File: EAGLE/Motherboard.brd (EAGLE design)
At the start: 60.9 x 49.2 mm, 16 parts, among them T1 BC337

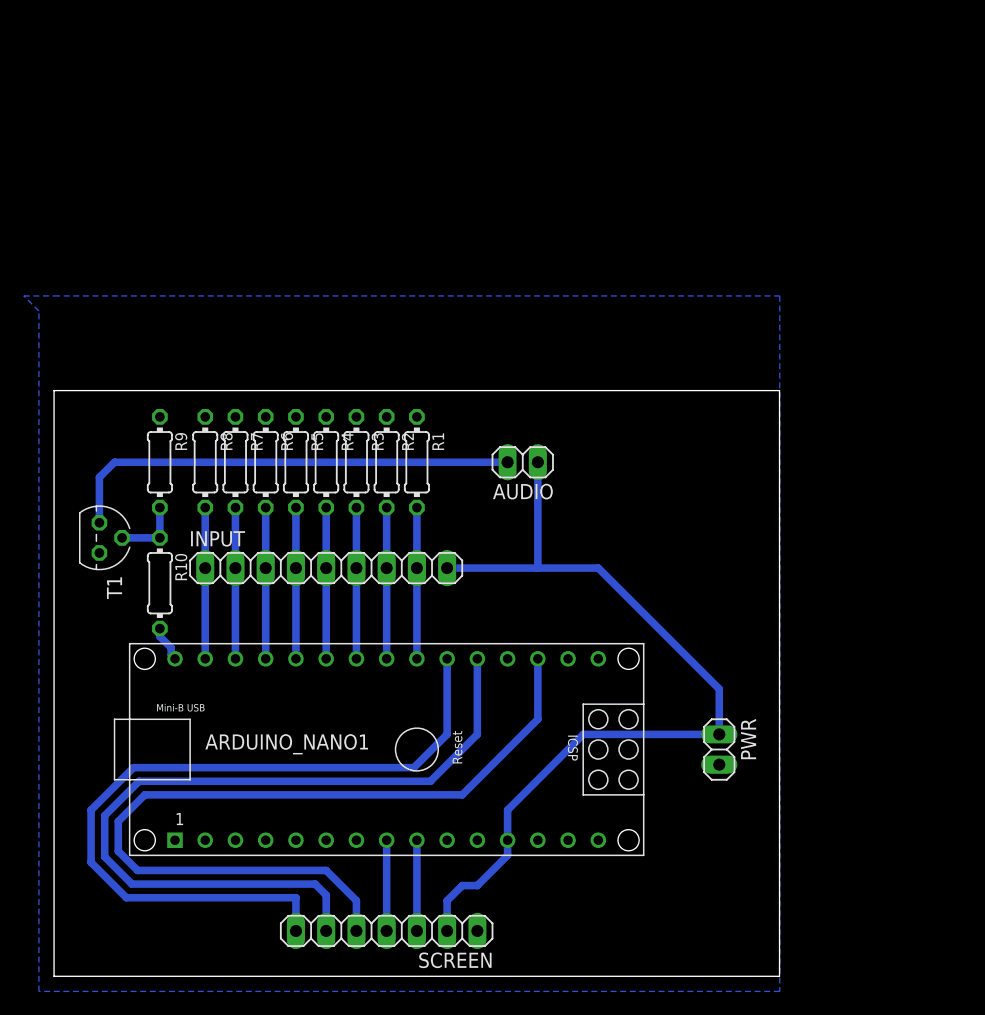
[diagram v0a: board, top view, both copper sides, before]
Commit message: Updated EAGLE schematics and board
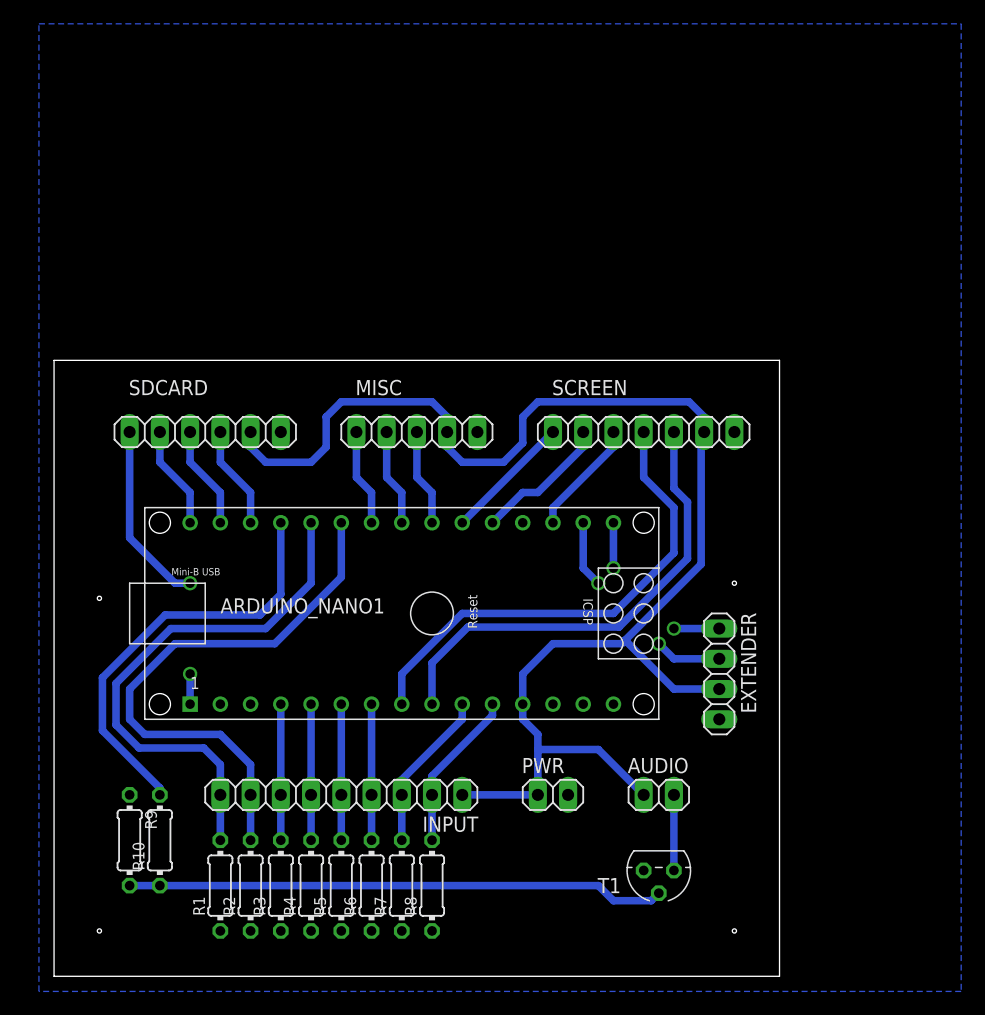
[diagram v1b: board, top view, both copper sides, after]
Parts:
- added EXTENDER: (no value), pinhead:1X04
- added MISC: (no value), pinhead:1X05
- added SDCARD: (no value), pinhead:1X06
- moved T1 54.7 mm to (50.8, 8.89), turned to 180 degrees
- moved SCREEN 47.1 mm to (49.5, 45.7)
- moved R8 40.3 mm to (31.8, 7.62), turned to 90 degrees
- moved R1 39.2 mm to (14.0, 7.62), turned to 90 degrees
- moved R7 38.2 mm to (29.2, 7.62), turned to 90 degrees
- moved R2 37.4 mm to (16.5, 7.62), turned to 90 degrees
- moved R6 36.7 mm to (26.7, 7.62), turned to 90 degrees
- moved R3 36.1 mm to (19.1, 7.62), turned to 90 degrees
- moved R5 35.8 mm to (24.1, 7.62), turned to 90 degrees
- moved R4 35.6 mm to (21.6, 7.62), turned to 90 degrees
- moved R9 31.9 mm to (6.35, 11.4)
- moved AUDIO 30.2 mm to (50.8, 15.2), turned to 0 degrees
- moved R10 21.6 mm to (8.89, 11.4), turned to 90 degrees
- moved INPUT 19.1 mm to (24.1, 15.2), turned to 180 degrees
- moved PWR 14.5 mm to (41.9, 15.2), turned to 0 degrees
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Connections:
- net N$1 renamed A5
- net N$2 renamed A4
- net N$3 renamed RST
- removed net N$10: ARDUINO_NANO1.28, INPUT.2, R7.2
- removed net N$11: ARDUINO_NANO1.29, INPUT.1, R8.2
- removed net N$15: ARDUINO_NANO1.30, R10.2
- removed net N$4: ARDUINO_NANO1.22, INPUT.8, R1.2
- removed net N$5: ARDUINO_NANO1.23, INPUT.7, R2.2
- removed net N$6: ARDUINO_NANO1.24, INPUT.6, R3.2
- removed net N$7: ARDUINO_NANO1.25, INPUT.5, R4.2
- removed net N$8: ARDUINO_NANO1.26, INPUT.4, R5.2
- removed net N$9: ARDUINO_NANO1.27, INPUT.3, R6.2
- new net A0: ARDUINO_NANO1.4, INPUT.7, R3.2
- new net A1: ARDUINO_NANO1.5, INPUT.6, R4.2
- new net A2: ARDUINO_NANO1.6, INPUT.5, R5.2
- new net A3: ARDUINO_NANO1.7, INPUT.4, R6.2
- new net A6: ARDUINO_NANO1.10, INPUT.3, R7.2
- new net A7: ARDUINO_NANO1.11, INPUT.2, R8.2
- new net D10: ARDUINO_NANO1.28, SDCARD.4
- new net D11: ARDUINO_NANO1.29, SDCARD.3
- new net D12: ARDUINO_NANO1.30, SDCARD.2
- new net D13: ARDUINO_NANO1.1, SDCARD.1
- new net D4: ARDUINO_NANO1.22, MISC.3
- new net D5: ARDUINO_NANO1.23, MISC.4
- new net D6: ARDUINO_NANO1.24, MISC.5
- new net D7: ARDUINO_NANO1.25, INPUT.8, R2.2
- new net D8: ARDUINO_NANO1.26, INPUT.9, R1.2
- new net D9: ARDUINO_NANO1.27, R10.2
- new net RX: ARDUINO_NANO1.17, EXTENDER.2
- new net TX: ARDUINO_NANO1.16, EXTENDER.1
- net GND: now also EXTENDER.4, MISC.1, SDCARD.6
- net VCC: now also EXTENDER.3, INPUT.1, MISC.2, SDCARD.5; no longer INPUT.9
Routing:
- net RST: track 70.6 -> 9.72 mm
- net D2: track 66.9 -> 11.5 mm
- net D3: track 64.5 -> 10.8 mm
- net D7: track 0.00 -> 46.9 mm
- net VCC: track 73.2 -> 119.4 mm
- net D8: track 0.00 -> 44.9 mm
- net N$13: track 5.71 -> 45.2 mm
- net D9: track 0.00 -> 35.7 mm
- net A4: track 7.62 -> 40.8 mm
- net N$12: track 38.6 -> 6.35 mm
- net A5: track 7.62 -> 39.7 mm
- net D13: track 0.00 -> 18.1 mm, vias 0 -> 2
- net A7: track 0.00 -> 13.5 mm
- net A6: track 0.00 -> 13.5 mm
- net N$9: track 12.7 -> 0.00 mm
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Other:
- board size 60.9 x 49.2 mm -> 60.9 x 51.7 mm

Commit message: Updated motherboard schetch and board design
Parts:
- added C1, C2: (no value), rcl:E2,5-6
- moved T1 14.2 mm to (36.8, 6.35), turned to 90 degrees
- moved AUDIO 12.7 mm to (43.2, 5.08), turned to 180 degrees
- moved PWR 1.27 mm to (43.2, 15.2)
- moved R10 1.27 mm to (8.89, 10.2)
- moved R9 1.27 mm to (6.35, 10.2)
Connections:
- net GND: now also C1.-, C2.-
- net VCC: now also C1.+, C2.+
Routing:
- net N$13: track 45.2 -> 28.6 mm
- net VCC: track 119.4 -> 134.9 mm
- net N$12: track 6.35 -> 5.08 mm
- net D9: track 35.7 -> 37.0 mm

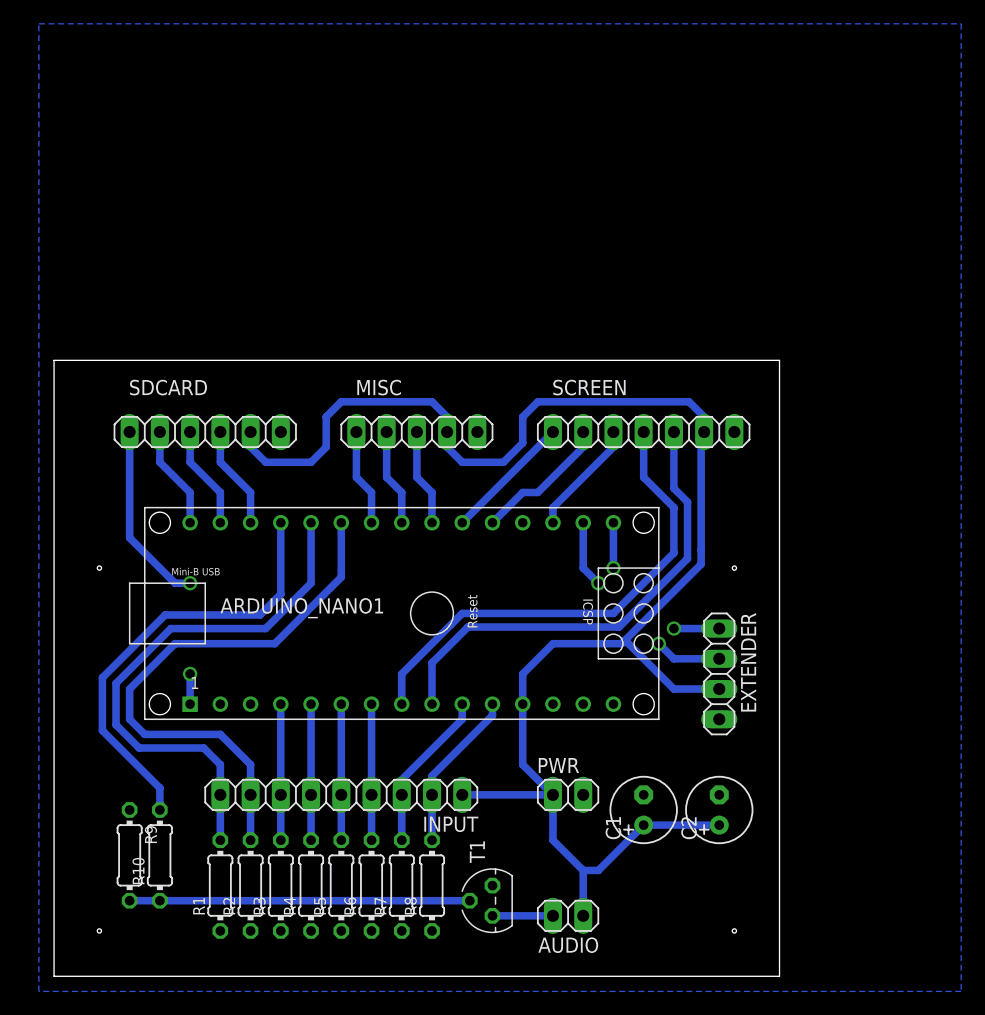
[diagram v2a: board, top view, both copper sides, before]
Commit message: * Redid the board design * Repinned a lot
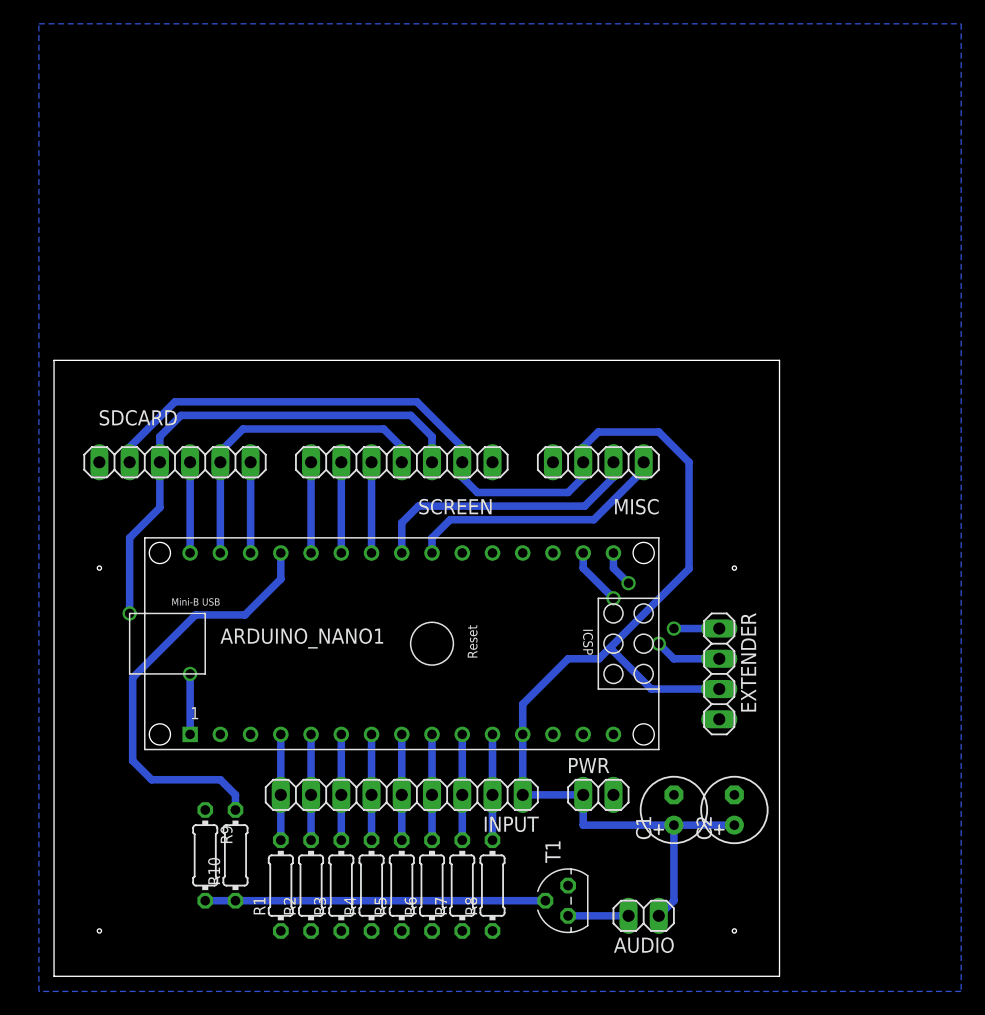
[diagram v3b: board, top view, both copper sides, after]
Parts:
- MISC: device pinhead:1X05 -> pinhead:1X04
- moved SCREEN 20.5 mm to (29.2, 43.2), turned to 0 degrees
- moved MISC 15.5 mm to (45.7, 43.2), turned to 0 degrees
- moved AUDIO 6.35 mm to (49.5, 5.08)
- moved T1 6.35 mm to (43.2, 6.35)
- moved R10 6.35 mm to (15.2, 10.2)
- moved R9 6.35 mm to (12.7, 10.2)
- moved INPUT 5.08 mm to (29.2, 15.2)
- moved R4 5.08 mm to (26.7, 7.62)
- moved R5 5.08 mm to (29.2, 7.62)
- moved R1 5.08 mm to (19.1, 7.62)
- moved R2 5.08 mm to (21.6, 7.62)
- moved R3 5.08 mm to (24.1, 7.62)
- moved R6 5.08 mm to (31.8, 7.62)
- moved R7 5.08 mm to (34.3, 7.62)
- moved R8 5.08 mm to (36.8, 7.62)
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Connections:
- net A0: now also INPUT.9, R1.2; no longer INPUT.7, R3.2
- net A1: now also INPUT.8, R2.2; no longer INPUT.6, R4.2
- net A2: now also INPUT.7, R3.2; no longer INPUT.5, R5.2
- net A3: now also INPUT.6, R4.2; no longer INPUT.4, R6.2
- net A4: now also INPUT.5, R5.2; no longer SCREEN.4
- net A5: now also INPUT.4, R6.2; no longer SCREEN.3
- net D10: now also SDCARD.6; no longer SDCARD.4
- net D11: now also SCREEN.4, SDCARD.5; no longer SDCARD.3
- net D12: now also SDCARD.4; no longer SDCARD.2
- net D13: now also SCREEN.5, SDCARD.3; no longer SDCARD.1
- net D2: no longer SCREEN.6
- net D3: no longer SCREEN.7
- net D4: now also MISC.4; no longer MISC.3
- net D5: now also MISC.3; no longer MISC.4
- net D6: now also SCREEN.3; no longer MISC.5
- net D7: now also SCREEN.2; no longer INPUT.8, R2.2
- net D8: now also SCREEN.1; no longer INPUT.9, R1.2
- net GND: now also SCREEN.7, SDCARD.1; no longer SCREEN.1, SDCARD.6
- net RST: no longer SCREEN.5
- net VCC: now also SCREEN.6, SDCARD.2; no longer SCREEN.2, SDCARD.5
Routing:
- net D7: track 46.9 -> 7.62 mm
- net D8: track 44.9 -> 7.62 mm
- net A4: track 40.8 -> 8.89 mm
- net A5: track 39.7 -> 8.89 mm
- net D13: track 18.1 -> 47.5 mm
- net D11: track 8.67 -> 26.4 mm
- net D5: track 8.15 -> 23.2 mm
- net D4: track 8.15 -> 22.1 mm
- net D2: track 11.5 -> 0.00 mm
- net D3: track 10.8 -> 0.00 mm
- net RST: track 9.72 -> 0.00 mm
- net A7: track 13.5 -> 8.89 mm
- net A6: track 13.5 -> 8.89 mm
- net A3: track 11.4 -> 8.89 mm
- net A2: track 11.4 -> 8.89 mm
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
